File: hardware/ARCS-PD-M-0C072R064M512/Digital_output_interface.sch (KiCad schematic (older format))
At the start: 89 parts

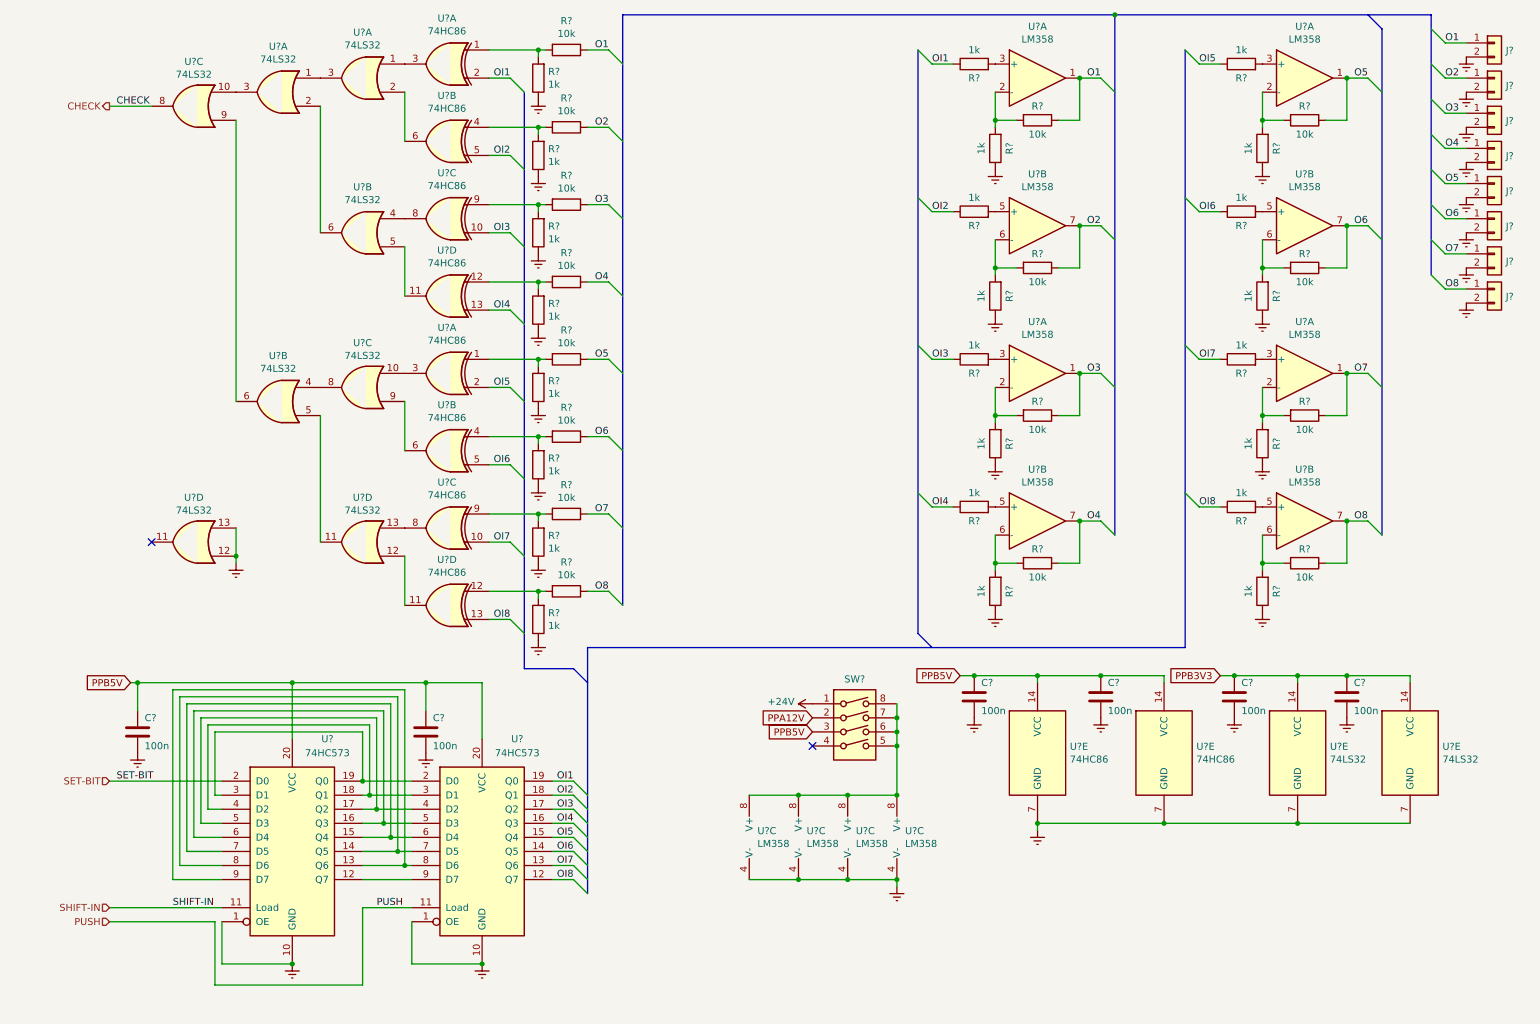
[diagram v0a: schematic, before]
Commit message: Create cards for input and output interface.
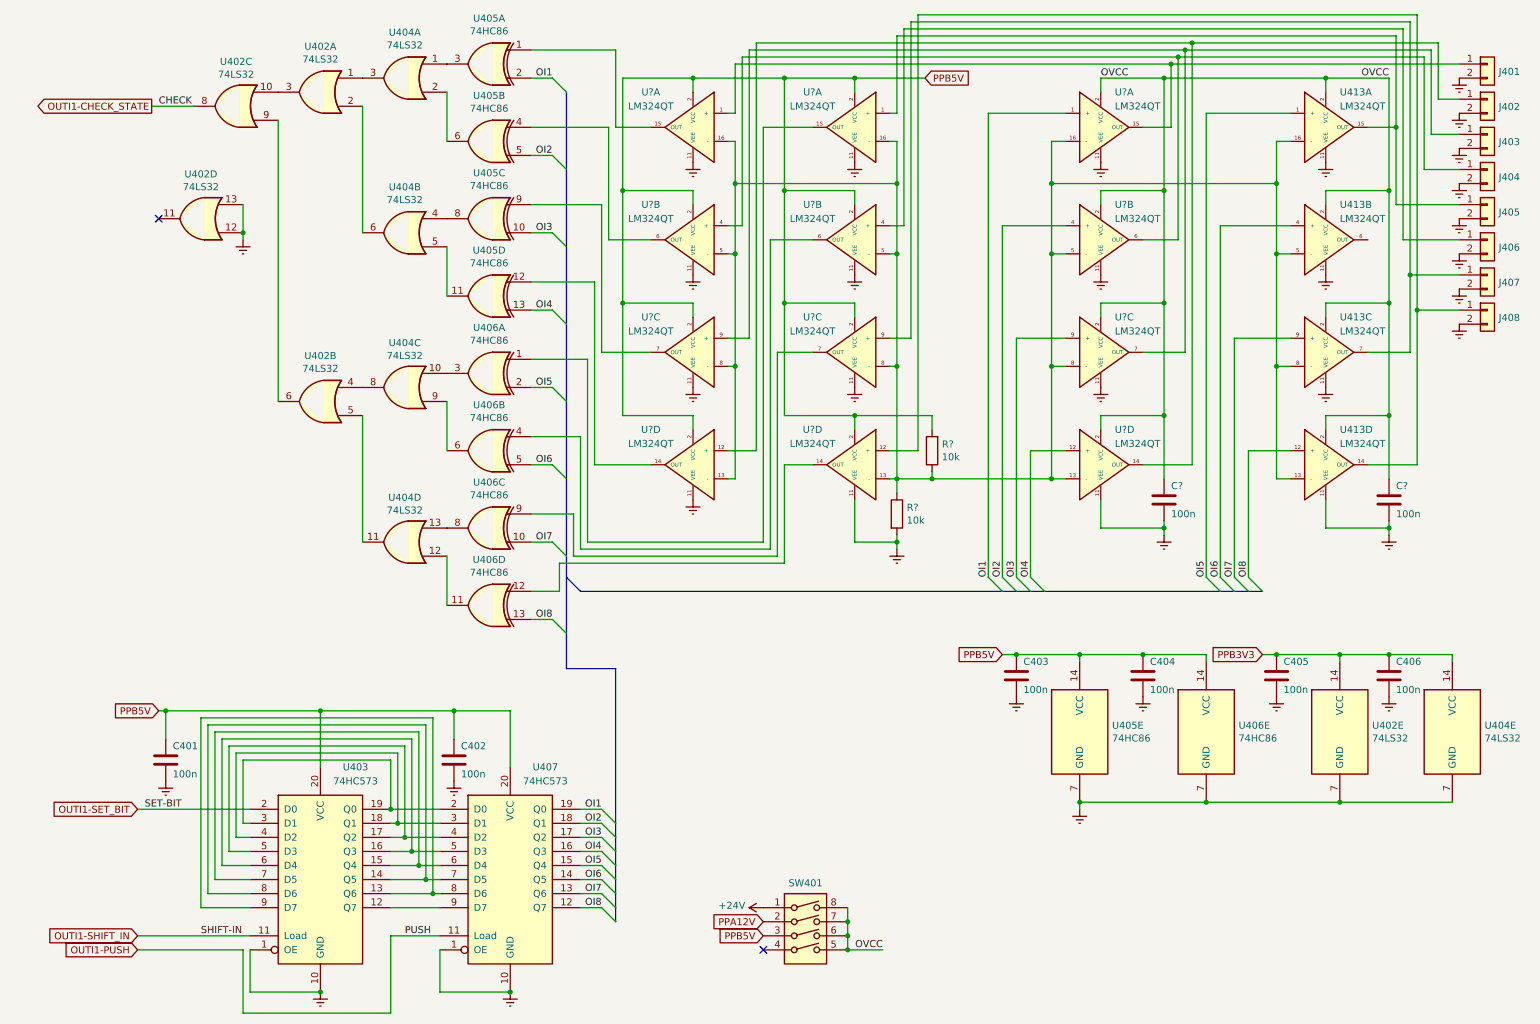
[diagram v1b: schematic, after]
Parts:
- removed R? (x16): 10k, symbol Device:R
- removed R? (x24): 1k, symbol Device:R
- removed U? (x12): LM358, symbol Amplifier_Operational:LM358
- added C? (x2): 100n, symbol Device:C
- added R? (x2): 10k, symbol Device:R
- added U413, U? (x12): LM324QT, symbol OPAmps:LM324QT
- gave numbers to parts that had none: 21
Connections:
- net Earth: now also C?.2, C?.2, R?.2, U413.11 (VEE), U413.11 (VEE), U413.11 (VEE), U413.11 (VEE), U?.11 (VEE), U?.11 (VEE), U?.11 (VEE), U?.11 (VEE), U?.11 (VEE), U?.11 (VEE), U?.11 (VEE), U?.11 (VEE), U?.11 (VEE), U?.11 (VEE), U?.11 (VEE), U?.11 (VEE)
- net OI1: now also U?.1 (+)
- net OI2: now also U?.4 (+)
- net OI3: now also U?.9 (+)
- net OI4: now also U?.12 (+)
- net OI5: now also U413.1 (+)
- net OI6: now also U413.4 (+)
- net OI7: now also U413.9 (+)
- net OI8: now also U413.12 (+)
- net PPB5V: now also R?.2, U?.2 (VCC), U?.2 (VCC), U?.2 (VCC), U?.2 (VCC), U?.2 (VCC), U?.2 (VCC), U?.2 (VCC), U?.2 (VCC)
- net OVCC: now reaches SW401.5, SW401.6, SW401.7, SW401.8
- net OVCC: now also C?.1, C?.1, U413.2 (VCC), U413.2 (VCC), U413.2 (VCC), U413.2 (VCC), U?.2 (VCC), U?.2 (VCC), U?.2 (VCC), U?.2 (VCC)
- net at U405.1: now also U?.15 (OUT)
- net at U405.4: now also U?.6 (OUT)
- net at U405.9: now also U?.7 (OUT)
- net at U405.12: now also U?.14 (OUT)
- net at U406.1: now also U?.15 (OUT)
- net at U406.4: now also U?.6 (OUT)
- net at U406.9: now also U?.7 (OUT)
- net at U406.12: now also U?.14 (OUT)
- net CHECK renamed OUTI1-CHECK_STATE
- net O1: no longer names the net of J401.1 (Pin_1)
- net O1: now also U?.1 (+), U?.15 (OUT)
- net O2: no longer names the net of J402.1 (Pin_1)
- net O2: now also U?.12 (+), U?.14 (OUT)
- net O3: no longer names the net of J403.1 (Pin_1)
- net O3: now also U?.7 (OUT), U?.9 (+)
- net O4: no longer names the net of J404.1 (Pin_1)
- net O4: now also U?.4 (+), U?.6 (OUT)
- net O5: no longer names the net of J405.1 (Pin_1)
- net O5: now also U413.15 (OUT), U?.1 (+)
- net O6: no longer names the net of J406.1 (Pin_1)
- net O6: now also U?.4 (+)
- net O7: no longer names the net of J407.1 (Pin_1)
- net O7: now also U413.7 (OUT), U?.9 (+)
- net O8: no longer names the net of J408.1 (Pin_1)
- net O8: now also U413.14 (OUT), U?.12 (+)
- net PUSH renamed OUTI1-PUSH
- net SET-BIT renamed OUTI1-SET_BIT
- net SHIFT-IN renamed OUTI1-SHIFT_IN
- new net: R?.1, R?.1, U413.13 (-), U413.16 (-), U413.5 (-), U413.8 (-), U?.13 (-), U?.13 (-), U?.13 (-), U?.16 (-), U?.16 (-), U?.16 (-), U?.5 (-), U?.5 (-), U?.5 (-), U?.8 (-), U?.8 (-), U?.8 (-)
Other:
- moved on the sheet: C401, C402, C403, C404, C405, C406, J401, J402, J403, J404, J405, J406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
